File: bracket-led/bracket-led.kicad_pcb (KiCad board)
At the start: 2 copper layers, 27 x 7 mm, 1 part, among them J1 BM08B-SURS-TF(LF)(SN)

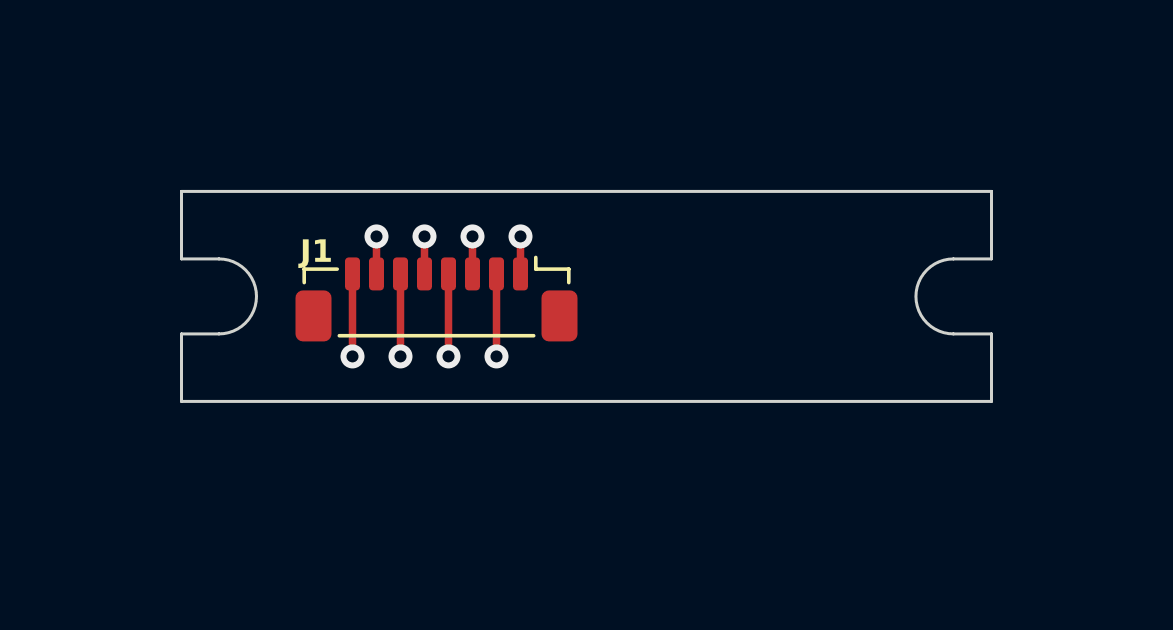
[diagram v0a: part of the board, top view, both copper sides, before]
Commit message: LED PCB perpendicular to bracket
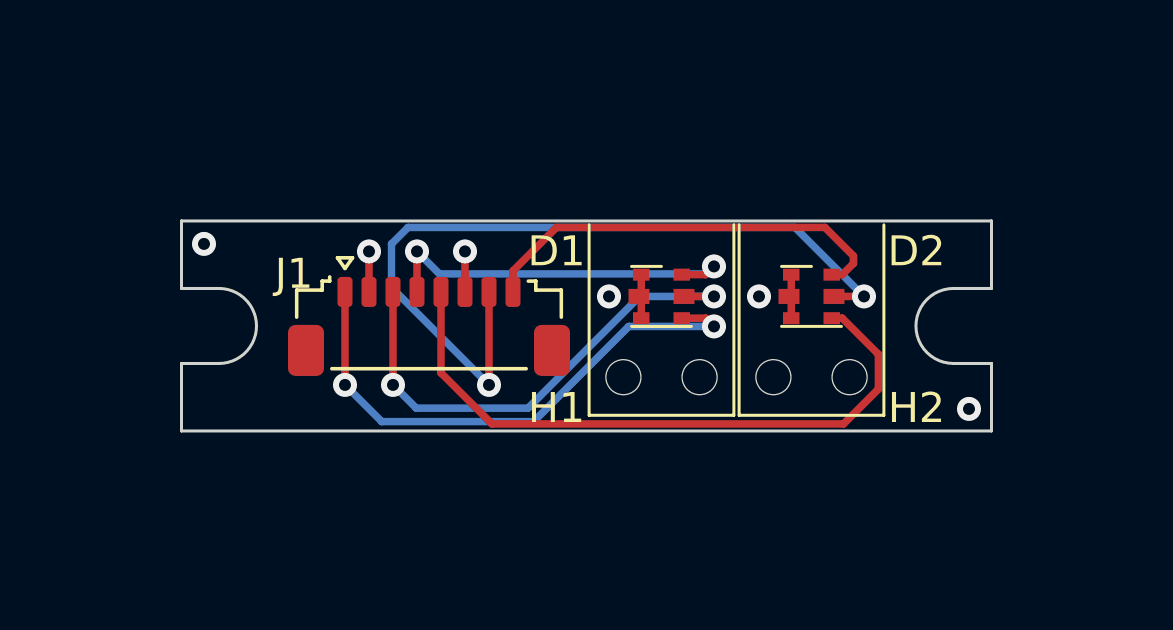
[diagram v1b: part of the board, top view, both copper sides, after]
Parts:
- added D1: LED_RGB, Open Ephys:EVERLIGHT_6-SMD-1.6x1.6, F.Cu at (47.5, 50.0)
- added D2: LED_RGB, Open Ephys:EVERLIGHT_6-SMD-1.6x1.6, F.Cu at (52.5, 50.0)
- added H1: SLP3-150-100-R, Open Ephys:SLP3-150-100-R, F.Cu at (47.5, 52.7)
- added H2: SLP3-150-100-R, Open Ephys:SLP3-150-100-R, F.Cu at (52.5, 52.7)
- J1: value BM08B-SURS-TF(LF)(SN) -> SM08B-SURS-TF(LF)(SN); footprint jonnew:JST_BM08B-SURS-TF(LF)(SN) -> Open Ephys:JST_SM08B-SURS-TF(LF)(SN)
- moved J1 1.03 mm to (39.8, 51.0), turned to 0 degrees
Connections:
- J1 pad 1: /B2 -> /G1
- J1 pad 2: /R2 -> GND
- J1 pad 3: GND -> /R1
- J1 pad 4: /G2 -> /B1
- J1 pad 5: /B1 -> /G2
- J1 pad 6: /R1 -> GND
- J1 pad 7: GND -> /R2
- J1 pad 8: /G1 -> /B2
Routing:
- net /R2: track 2.75 -> 27.1 mm, vias 1 -> 2
- net /G2: track 2.75 -> 21.7 mm, vias 1 -> 0
- net /G1: track 2.75 -> 18.4 mm, vias 1 -> 2
- net /R1: track 2.75 -> 16.7 mm, vias 1 -> 2
- net /B2: track 1.33 -> 14.2 mm, vias 1 -> 0
- net /B1: track 1.25 -> 12.9 mm, vias 1 -> 2
- net GND: track 2.50 -> 5.60 mm, vias 2 -> 6
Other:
- board text added: "Rev. A"
- board text removed: "locked"

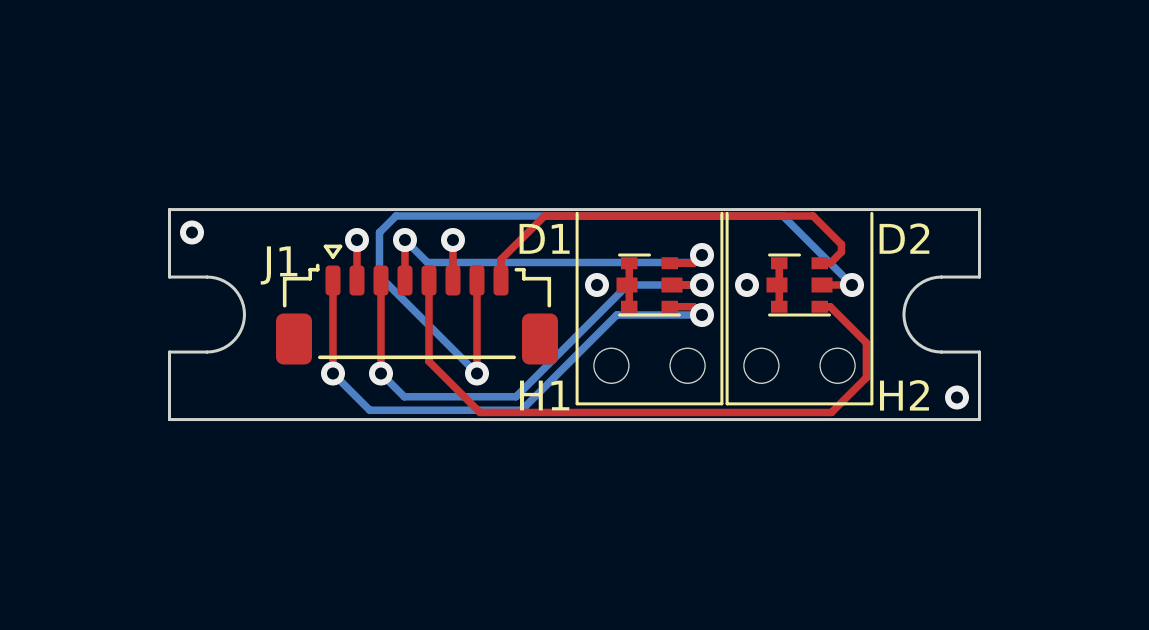
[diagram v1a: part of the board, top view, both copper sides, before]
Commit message: added logo for engraving if we want
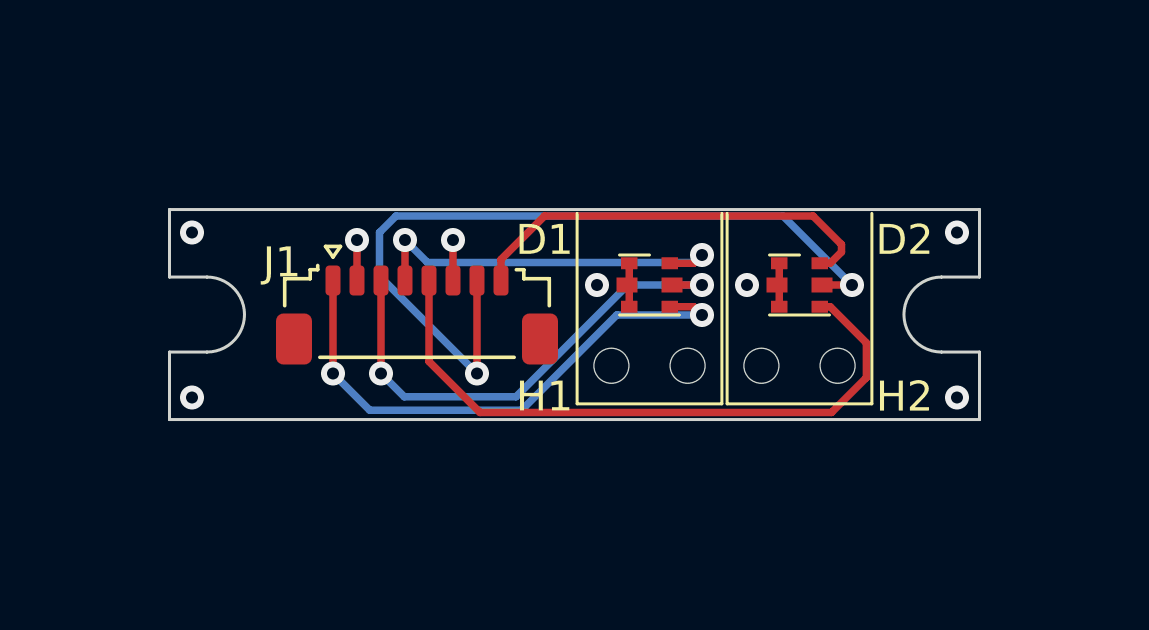
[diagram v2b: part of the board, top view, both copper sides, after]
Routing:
- net GND: vias 6 -> 8
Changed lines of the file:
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@@
   (gr_line (start 32.75 49.73476) (end 31.5 49.73476)
     (stroke (width 0.1) (type default)) (layer "Edge.Cuts"))
-  (gr_text "Rev. A" (at 31.75 54.25) (layer "F.Mask")
+  (gr_text "Rev. A" (at 34.5 54.25) (layer "F.Mask")
     (effects (font (size 0.5 0.5) (thickness 0.125)) (justify left bottom))
   )
@@
   (via (at 45.75 50) (size 0.8) (drill 0.4) (layers "F.Cu" "B.Cu") (free) (net 7))
   (via (at 57.75 53.75) (size 0.8) (drill 0.4) (layers "F.Cu" "B.Cu") (free) (net 7))
+  (via (at 32.25 53.75) (size 0.8) (drill 0.4) (layers "F.Cu" "B.Cu") (free) (net 7))
   (via (at 32.25 48.25) (size 0.8) (drill 0.4) (layers "F.Cu" "B.Cu") (free) (net 7))
   (via (at 50.75 50) (size 0.8) (drill 0.4) (layers "F.Cu" "B.Cu") (free) (net 7))
   (via (at 37.75 48.5) (size 0.8) (drill 0.4) (layers "F.Cu" "B.Cu") (net 7))
+  (via (at 57.75 48.25) (size 0.8) (drill 0.4) (layers "F.Cu" "B.Cu") (free) (net 7))
   (via (at 40.95 48.5) (size 0.8) (drill 0.4) (layers "F.Cu" "B.Cu") (net 7))
   (zone (net 7) (net_name "GND") (layers "F&B.Cu") (hatch edge 0.5)
     (connect_pads (clearance 0.25))
     (min_thickness 0.25) (filled_areas_thickness no)
-    (fill yes (thermal_gap 0.25) (thermal_bridge_width 0.25) (smoothing fillet) (radius 1))
+    (fill yes (thermal_gap 0.25) (thermal_bridge_width 0.25))
     (polygon
       (pts
